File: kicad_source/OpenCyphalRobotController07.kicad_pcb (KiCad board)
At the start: 2 copper layers, 100 x 60 mm, 107 parts, among them CN1 ADAFRUIT_FEATHER, P1 WR-TBL_691313710002, P2 WR-TBL_691322310002, P3 WR-TBL_691313710002, P4 WR-TBL_691313710002, Q1 2N7002, Q2 IPD90P03P4L- 04, U1 IFX007T, U2 74xx08, U3 IFX007T, U4 IFX007T, U5 IFX007T, U6 OPA2374AIDCN, U7 OPA2374AIDCN, U8 ADS1015, U9 IFX91041EFJ

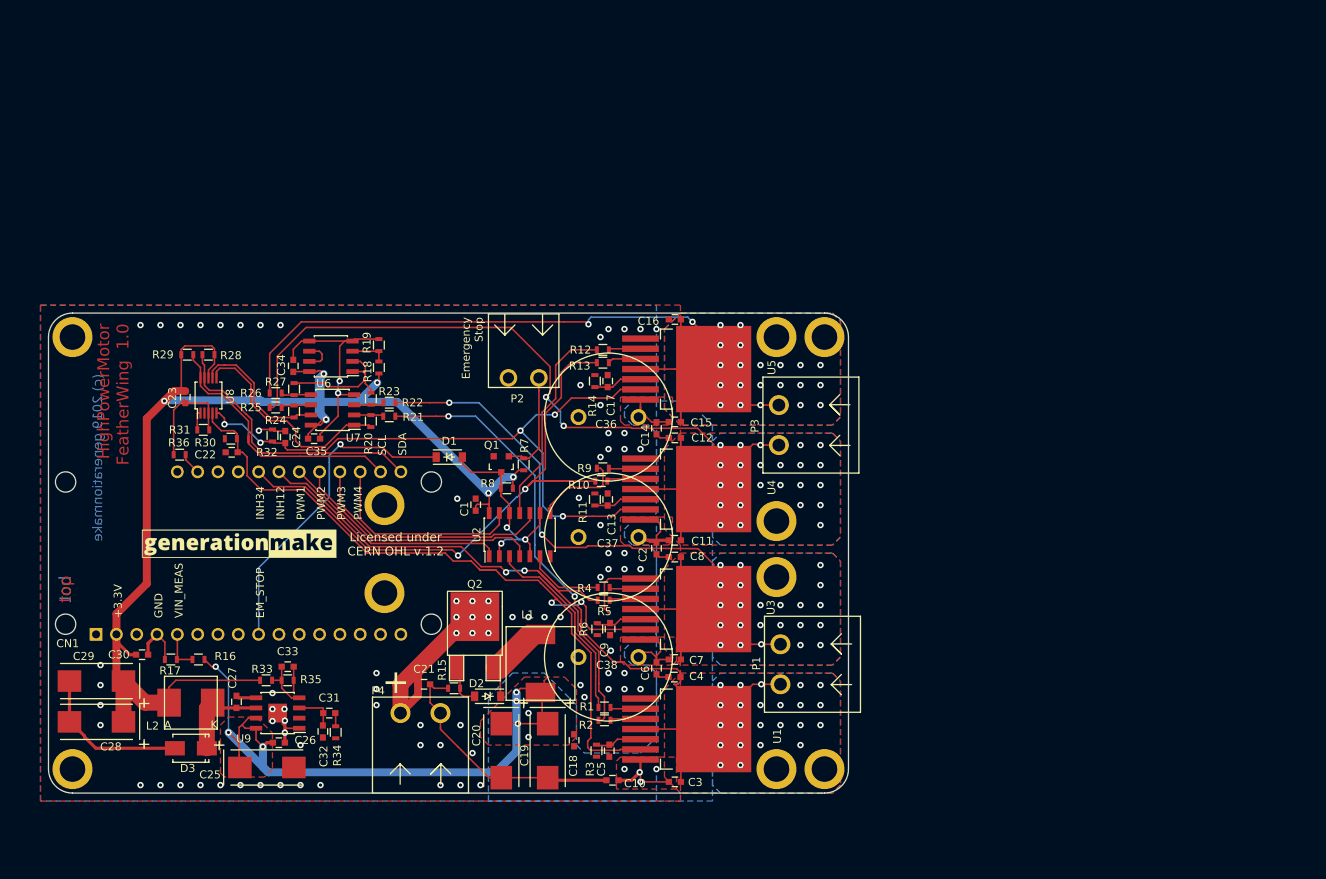
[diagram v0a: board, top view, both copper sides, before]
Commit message: updated layout
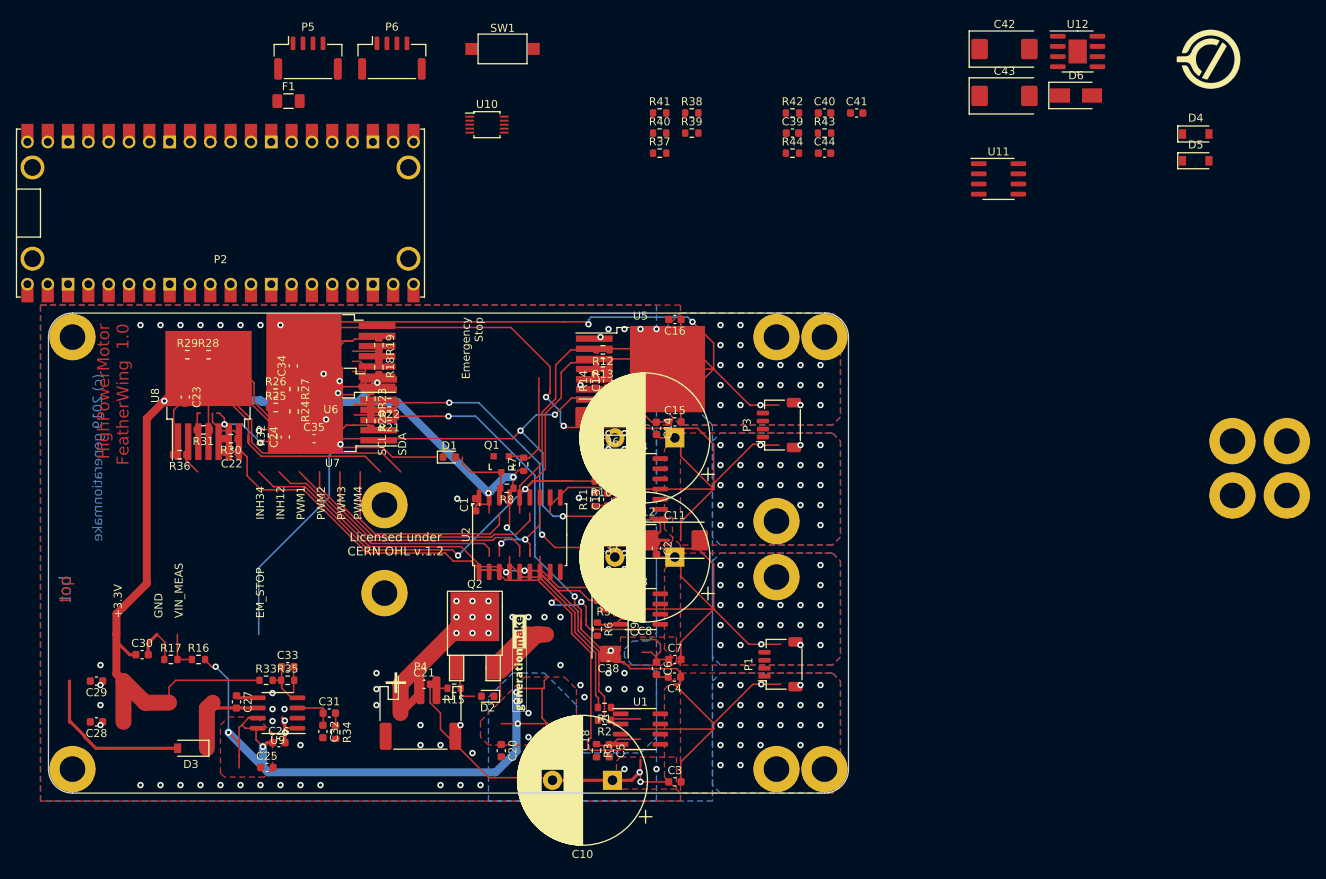
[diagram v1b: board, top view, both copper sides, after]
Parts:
- removed CN1: ADAFRUIT_FEATHER, MODULE_compute:ADAFRUIT_FEATHER_HOLES
- removed G*** (x2): generationmake_logo, labels:generationmake_logo
- added C39: 100nF, Capacitor_SMD:C_0603_1608Metric, F.Cu at (144.0, 43.5)
- added C40: 470pF, Capacitor_SMD:C_0603_1608Metric, F.Cu at (148.0, 41.0)
- added C41: 220nF, Capacitor_SMD:C_0603_1608Metric, F.Cu at (152.0, 41.0)
- added C42: 330uF 6.3V, Capacitor_Tantalum_SMD:CP_EIA-7343-15_Kemet-W, F.Cu at (170.5, 33.0)
- added C43: 330uF 6.3V, Capacitor_Tantalum_SMD:CP_EIA-7343-15_Kemet-W, F.Cu at (170.5, 38.9)
- added C44: 100nF, Capacitor_SMD:C_0603_1608Metric, F.Cu at (148.0, 46.0)
- added D4: 10V, Diode_SMD:D_SOD-123, F.Cu at (194.4, 43.6)
- added D5: BAT46W, Diode_SMD:D_SOD-123, F.Cu at (194.4, 47.0)
- added D6: SSA34, Diode_SMD:D_SMA, F.Cu at (179.4, 38.8)
- added F1: nanoSMDC050F, Fuse:Fuse_1206_3216Metric, F.Cu at (81.0, 39.5)
- added L3: Label, generationmake:opencyphal_small, F.Cu at (196.0, 34.3)
- added MECH11: MHP_3.2_5.0, generationmake:MHP_3.2_5.8, F.Cu at (199.0, 82.0)
- added MECH12: MHP_3.2_5.0, generationmake:MHP_3.2_5.8, F.Cu at (199.0, 88.8)
- added MECH13: MHP_3.2_5.0, generationmake:MHP_3.2_5.8, F.Cu at (205.8, 82.0)
- added MECH14: MHP_3.2_5.0, generationmake:MHP_3.2_5.8, F.Cu at (205.8, 88.8)
- added P5: SM04B-GHS-TB, Connector_JST:JST_GH_SM04B-GHS-TB_1x04-1MP_P1.25mm_Horizontal, F.Cu at (83.4, 34.1)
- added P6: SM04B-GHS-TB, Connector_JST:JST_GH_SM04B-GHS-TB_1x04-1MP_P1.25mm_Horizontal, F.Cu at (93.9, 34.1)
- added R37: 2k2, Resistor_SMD:R_0603_1608Metric, F.Cu at (127.4, 46.0)
- added R38: 2k2, Resistor_SMD:R_0603_1608Metric, F.Cu at (131.4, 41.0)
- added R39: 2k2, Resistor_SMD:R_0603_1608Metric, F.Cu at (131.4, 43.5)
- added R40: 150k, Resistor_SMD:R_0603_1608Metric, F.Cu at (127.4, 43.5)
- added R41: 10k, Resistor_SMD:R_0603_1608Metric, F.Cu at (127.4, 41.0)
- added R42: 22k, Resistor_SMD:R_0603_1608Metric, F.Cu at (144.0, 41.0)
- added R43: 10k, Resistor_SMD:R_0603_1608Metric, F.Cu at (148.0, 43.5)
- added R44: 2k2, Resistor_SMD:R_0603_1608Metric, F.Cu at (144.0, 46.0)
- added SW1: PTS636 SM43 SMTR LFS, Button_Switch_SMD:SW_SPST_CK_RS282G05A3, F.Cu at (107.8, 33.0)
- added U10: ADS1015IDGS, Package_SO:TSSOP-10_3x3mm_P0.5mm, F.Cu at (105.8, 42.5)
- added U11: OPA2374AIDCN, Package_SO:SOIC-8_3.9x4.9mm_P1.27mm, F.Cu at (169.8, 49.2)
- added U12: IFX91041EFJ, Package_SO:SOIC-8-1EP_3.9x4.9mm_P1.27mm_EP2.29x3mm, F.Cu at (179.6, 33.3)
- C1, C13, C14, C17, C18, C2, C30, C35, C6: footprint capacitors:C_0603 -> Capacitor_SMD:C_0603_1608Metric
- C10: value 100nF -> 1000uF 50V; footprint capacitors:C_0603 -> Capacitor_THT:CP_Radial_D16.0mm_P7.50mm
- C11: value 220nF -> 47uF 50V; footprint capacitors:C_0603 -> Capacitor_Tantalum_SMD:CP_EIA-7343-15_Kemet-W
- C12, C8: value 220nF -> 1000uF 50V; footprint capacitors:C_0603 -> Capacitor_THT:CP_Radial_D16.0mm_P7.50mm
- C15, C16, C27, C3, C7: value 220nF -> 100nF; footprint capacitors:C_0603 -> Capacitor_SMD:C_0603_1608Metric
- C19, C20, C25: value 47uF 50V -> 220nF; footprint capacitors:TantalC_SizeD_EIA-7343_Wave -> Capacitor_SMD:C_0603_1608Metric
- C21, C23, C26: value 100nF -> 220nF; footprint capacitors:C_0603 -> Capacitor_SMD:C_0603_1608Metric
- C22, C24: value 1nF -> 220nF; footprint capacitors:C_0603 -> Capacitor_SMD:C_0603_1608Metric
- C28, C29: value 330uF 6.3V -> 100nF; footprint capacitors:TantalC_SizeD_EIA-7343_Wave -> Capacitor_SMD:C_0603_1608Metric
- C31: value 22nF -> 100nF; footprint capacitors:C_0603 -> Capacitor_SMD:C_0603_1608Metric
- C32: value DNI -> 100nF; footprint capacitors:C_0603 -> Capacitor_SMD:C_0603_1608Metric
- C33: value 470pF -> 1nF; footprint capacitors:C_0603 -> Capacitor_SMD:C_0603_1608Metric
- C34: value 100nF -> 1nF; footprint capacitors:C_0603 -> Capacitor_SMD:C_0603_1608Metric
- C36: value 1000uF 50V -> 47uF 50V; footprint capacitors:C_elec_THT_16x25_RM7.5 -> Capacitor_Tantalum_SMD:CP_EIA-7343-15_Kemet-W
- C37: value 1000uF 50V -> DNI; footprint capacitors:C_elec_THT_16x25_RM7.5 -> Capacitor_SMD:C_0603_1608Metric
- C38: value 1000uF 50V -> 22nF; footprint capacitors:C_elec_THT_16x25_RM7.5 -> Capacitor_SMD:C_0603_1608Metric
- C4: value 220nF -> 10pF; footprint capacitors:C_0603 -> Capacitor_SMD:C_0603_1608Metric
- C5: value 100nF -> 10pF; footprint capacitors:C_0603 -> Capacitor_SMD:C_0603_1608Metric
- C9: value 100nF -> 47uF 50V; footprint capacitors:C_0603 -> Capacitor_Tantalum_SMD:CP_EIA-7343-15_Kemet-W
- D1: value BAT46W -> 150060RS75000; footprint diodes:SOD-123 -> LED_SMD:LED_0603_1608Metric
- D2: value 10V -> 150060YS75000; footprint diodes:SOD-123 -> LED_SMD:LED_0603_1608Metric
- D3: value SSA34 -> MBR0530T; footprint diodes:SMA_Standard -> Diode_SMD:D_SOD-123
- L1: value 744373580022 -> Label; footprint L_power:WE-LHMI80xx -> generationmake:generationmake_small_silk
- L2: value 74437346220 -> Label; footprint L_power:WE-LHMI70xx -> generationmake:generationmake_small_solder
- MECH1, MECH2, MECH3, MECH4: value MHP_3.2_5.0 -> MHP_3.2_5.8; footprint MECH_mounting_holes:MHP_3.2_5.0 -> generationmake:MHP_3.2_5.8
- MECH10, MECH5, MECH6, MECH7, MECH8, MECH9: footprint MECH_mounting_holes:MHP_3.2_5.0 -> generationmake:MHP_3.2_5.8
- P1, P3: value WR-TBL_691313710002 -> SM04B-SRSS-TB; footprint CON_wuerth:WR-TBL_691313710002 -> Connector_JST:JST_SH_SM04B-SRSS-TB_1x04-1MP_P1.00mm_Horizontal
- P2: value WR-TBL_691322310002 -> RASPBERRYPI_PICO; footprint CON_wuerth:WR-TBL_691322310002 -> generationmake:RASPI_PICO_SOLDER_ONLY
- P4: value WR-TBL_691313710002 -> S3B-PH-SM4-TB; footprint CON_wuerth:WR-TBL_691313710002 -> Connector_JST:JST_PH_S3B-PH-SM4-TB_1x03-1MP_P2.00mm_Horizontal
- R1, R10, R12, R13, R15, R17, R18, R19, R2, R28, R30, R4, R7, R8, R9: footprint resistors:R_0603 -> Resistor_SMD:R_0603_1608Metric
- R11, R14: value 510 -> 10k; footprint resistors:R_0603 -> Resistor_SMD:R_0603_1608Metric
- R16: value 150k -> 10k; footprint resistors:R_0603 -> Resistor_SMD:R_0603_1608Metric
- R20, R27: value 2k2 -> 10k; footprint resistors:R_0603 -> Resistor_SMD:R_0603_1608Metric
- R21, R22: value 56k -> 510; footprint resistors:R_0603 -> Resistor_SMD:R_0603_1608Metric
- R23, R24: value 2k2 -> 510; footprint resistors:R_0603 -> Resistor_SMD:R_0603_1608Metric
- R25, R26: value 56k -> 10k; footprint resistors:R_0603 -> Resistor_SMD:R_0603_1608Metric
- R29: value 10k -> DNI; footprint resistors:R_0603 -> Resistor_SMD:R_0603_1608Metric
- R3: value 510 -> 100k; footprint resistors:R_0603 -> Resistor_SMD:R_0603_1608Metric
- R31: value DNI -> 1k; footprint resistors:R_0603 -> Resistor_SMD:R_0603_1608Metric
- R32: value 1k -> 56k; footprint resistors:R_0603 -> Resistor_SMD:R_0603_1608Metric
- R33: value 10k -> 56k; footprint resistors:R_0603 -> Resistor_SMD:R_0603_1608Metric
- R34: value 22k -> 56k; footprint resistors:R_0603 -> Resistor_SMD:R_0603_1608Metric
- R35: value 2k2 -> 56k; footprint resistors:R_0603 -> Resistor_SMD:R_0603_1608Metric
- R36: value DNI -> 2k2; footprint resistors:R_0603 -> Resistor_SMD:R_0603_1608Metric
- R5: value 10k -> 3k3; footprint resistors:R_0603 -> Resistor_SMD:R_0603_1608Metric
- R6: value 510 -> 3k3; footprint resistors:R_0603 -> Resistor_SMD:R_0603_1608Metric
- U1: value IFX007T -> 24LC64-I/SN; footprint SOT_TO:TO-263-7Lead -> Package_SO:SOIC-8_3.9x4.9mm_P1.27mm
- U2: value 74xx08 -> MCP2515-I/SO; footprint SOIC:SOIC-14_3.9x8.7mm_Pitch1.27mm -> Package_SO:SOIC-18W_7.5x11.6mm_P1.27mm
- U3: value IFX007T -> SN65HVD232; footprint SOT_TO:TO-263-7Lead -> Package_SO:SOIC-8_3.9x4.9mm_P1.27mm
- U4: value IFX007T -> 74xx08; footprint SOT_TO:TO-263-7Lead -> Package_SO:SOIC-14_3.9x8.7mm_P1.27mm
- U5: footprint SOT_TO:TO-263-7Lead -> Package_TO_SOT_SMD:TO-263-7_TabPin8
- U6, U7: value OPA2374AIDCN -> IFX007T; footprint SOIC:SOIC-8_3.9x4.9mm_Pitch1.27mm -> Package_TO_SOT_SMD:TO-263-7_TabPin8
- U8: value ADS1015 -> IFX007T; footprint SSOP:MSOP-10_3x3mm_Pitch0.5mm -> Package_TO_SOT_SMD:TO-263-7_TabPin8
- U9: value IFX91041EFJ -> OPA2374AIDCN; footprint SOIC:SOIC-8-1EP_3.9x4.9mm_Pitch1.27mm -> Package_SO:SOIC-8_3.9x4.9mm_P1.27mm
- moved P2 43.1 mm to (72.5, 53.5), turned to 90 degrees
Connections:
- C1 pad 1: +3V3 -> +3.3V
- C10 pad 1: VIN -> +BATT
- C11 pad 1: VIN -> +BATT
- C11 pad 2: OUT3 -> GND
- C12 pad 1: OUT3 -> +BATT
- C13 pad 1: /MotorDriver/SR3 -> Net-(C13-Pad1)
- C14 pad 1: VIN -> +3.3V
- C15 pad 1: VIN -> /MotorDriver/SR1
- C15 pad 2: OUT4 -> GND
- C16 pad 1: OUT4 -> /MotorDriver/SR2
- C17 pad 1: /MotorDriver/SR4 -> /MotorDriver/SR3
- C18 pad 1: VIN -> /MotorDriver/SR4
- C19 pad 1: VIN -> +BATT
- C19 pad 2: GND -> OUT1
- C2 pad 1: VIN -> /+BATT_MEAS
- C20 pad 1: VIN -> OUT1
- C21 pad 1: Net-(C21-Pad1) -> +BATT
- C21 pad 2: GND -> OUT2
- C22 pad 1: IS12 -> OUT2
- C23 pad 1: +3V3 -> +BATT
- C23 pad 2: GND -> OUT3
- C24 pad 1: IS34 -> OUT3
- C25 pad 1: VIN -> +BATT
- C25 pad 2: GND -> OUT4
- C26 pad 1: VIN -> OUT4
- C27 pad 1: /VoltageRegulator/BDS -> +BATT
- C27 pad 2: /VoltageRegulator/BUO -> GND
- C28 pad 1: +3V3 -> +BATT
- C29 pad 1: +3V3 -> +BATT
- C3 pad 1: VIN -> +3.3V
- C3 pad 2: OUT1 -> GND
- C30 pad 1: +3V3 -> +BATT
- C31 pad 1: /VoltageRegulator/COMP -> +3.3V
- C31 pad 2: Net-(C31-Pad2) -> GND
- C32 pad 1: /VoltageRegulator/COMP -> +3.3V
- C33 pad 1: /VoltageRegulator/FB -> IS12
- C34 pad 1: +3V3 -> IS34
- C35 pad 1: +3V3 -> +3.3V
- C36 pad 1: VIN -> +BATT
- C37 pad 1: VIN -> /VoltageRegulator/COMP
- C38 pad 1: VIN -> /VoltageRegulator/COMP
- C38 pad 2: GND -> Net-(C38-Pad2)
- C4 pad 1: OUT1 -> /MCP2515/MCP2515_OSC2
- C5 pad 1: /MotorDriver/SR1 -> /MCP2515/MCP2515_OSC1
- C6 pad 1: VIN -> +3.3V
- C7 pad 1: VIN -> +BATT
- C7 pad 2: OUT2 -> GND
- C8 pad 1: OUT2 -> +BATT
- C9 pad 1: /MotorDriver/SR2 -> +BATT
- D1 pad 1: EM_STOP_D -> GND
- D1 pad 2: /MotorDriver/EM_STOP_Q -> /LED2_R
- D2 pad 1: Net-(D2-Pad1) -> GND
- D2 pad 2: Net-(D2-Pad2) -> /LED3_R
- D3 pad 1: /VoltageRegulator/BUO -> /MCP2515/CANVCC
- D3 pad 2: GND -> Net-(D3-Pad2)
- MECH1 pad 1: (no net) -> unconnected-(MECH1-Pad1)
- MECH10 pad 1: (no net) -> unconnected-(MECH10-Pad1)
- MECH2 pad 1: (no net) -> unconnected-(MECH2-Pad1)
- MECH3 pad 1: (no net) -> unconnected-(MECH3-Pad1)
- MECH4 pad 1: (no net) -> unconnected-(MECH4-Pad1)
- MECH5 pad 1: (no net) -> unconnected-(MECH5-Pad1)
- MECH6 pad 1: (no net) -> unconnected-(MECH6-Pad1)
- MECH7 pad 1: (no net) -> unconnected-(MECH7-Pad1)
- MECH8 pad 1: (no net) -> unconnected-(MECH8-Pad1)
- MECH9 pad 1: (no net) -> unconnected-(MECH9-Pad1)
- P1 pad 1: OUT1 -> GND
- P1 pad 2: OUT2 -> +3.3V
- P2 pad 1: /MotorDriver/EM_STOP -> /SER_TX
- P2 pad 2: GND -> /SER_RX
- P3 pad 1: OUT3 -> GND
- P3 pad 2: OUT4 -> +3.3V
- P4 pad 1: Net-(C21-Pad1) -> /NEOPIXEL_R
- P4 pad 2: GND -> +5V
- Q2 pad 1: Net-(D2-Pad2) -> Net-(D4-Pad2)
- Q2 pad 2: Net-(C21-Pad1) -> Net-(C13-Pad1)
- Q2 pad 3: Net-(D2-Pad1) -> Net-(D4-Pad1)
- R1 pad 1: /MotorDriver/PWM1_R -> +3.3V
- R1 pad 2: /MotorDriver/PWM1_U -> I2C_SCL
- R10 pad 1: /MotorDriver/INH3_R -> +3.3V
- R10 pad 2: INH34 -> /MotorDriver/EM_STOP
- R11 pad 1: /MotorDriver/SR3 -> Net-(D4-Pad2)
- R12 pad 1: /MotorDriver/PWM4_R -> +3.3V
- R12 pad 2: /MotorDriver/PWM4_U -> /MotorDriver/EM_STOP_Q
- R13 pad 1: /MotorDriver/INH4_R -> /MotorDriver/PWM1_R
- R13 pad 2: INH34 -> /MotorDriver/PWM1_U
- R14 pad 1: /MotorDriver/SR4 -> /MotorDriver/INH1_R
- R14 pad 2: GND -> INH12
- R15 pad 1: Net-(D2-Pad2) -> /MotorDriver/PWM2_R
- R15 pad 2: GND -> /MotorDriver/PWM2_U
- R16 pad 1: VIN_MEAS -> /MotorDriver/INH2_R
- R16 pad 2: VIN -> INH12
- R17 pad 1: GND -> /MotorDriver/PWM3_R
- R17 pad 2: VIN_MEAS -> /MotorDriver/PWM3_U
- R18 pad 1: /Measurement/VREF_IN -> /MotorDriver/INH3_R
- R18 pad 2: +3V3 -> INH34
- R19 pad 1: GND -> /MotorDriver/PWM4_R
- R19 pad 2: /Measurement/VREF_IN -> /MotorDriver/PWM4_U
- R2 pad 1: /MotorDriver/INH1_R -> +3.3V
- R2 pad 2: INH12 -> I2C_SDA
- R20 pad 1: /Measurement/OUT1R -> /MotorDriver/INH4_R
- R20 pad 2: /Measurement/VS12 -> INH34
- R21 pad 1: OUT1 -> /MotorDriver/SR1
- R21 pad 2: /Measurement/OUT1R -> GND
- R22 pad 1: OUT2 -> /MotorDriver/SR2
- R22 pad 2: /Measurement/OUT2R -> GND
- R23 pad 1: /Measurement/VREF -> /MotorDriver/SR3
- R23 pad 2: /Measurement/OUT2R -> GND
- R24 pad 1: /Measurement/OUT3R -> /MotorDriver/SR4
- R24 pad 2: /Measurement/VS34 -> GND
- R25 pad 1: OUT3 -> /Measurement/VREF_IN
- R25 pad 2: /Measurement/OUT3R -> +3.3V
- R26 pad 1: OUT4 -> GND
- R26 pad 2: /Measurement/OUT4R -> /Measurement/VREF_IN
- R27 pad 1: /Measurement/VREF -> I2C_SDA
- R27 pad 2: /Measurement/OUT4R -> +3.3V
- R28 pad 1: I2C_SDA -> +3.3V
- R28 pad 2: +3V3 -> I2C_SCL
- R29 pad 1: +3V3 -> GND
- R29 pad 2: I2C_SCL -> /Measurement/ADDR
- R3 pad 1: /MotorDriver/SR1 -> +5V
- R3 pad 2: GND -> /+BATT_MEAS
- R31 pad 1: GND -> IS34
- R31 pad 2: /Measurement/ADDR -> GND
- R32 pad 1: IS34 -> OUT1
- R32 pad 2: GND -> /Measurement/OUT1R
- R33 pad 1: +3V3 -> OUT2
- R33 pad 2: /VoltageRegulator/FB -> /Measurement/OUT2R
- R34 pad 1: Net-(C31-Pad2) -> OUT3
- R34 pad 2: GND -> /Measurement/OUT3R
- R35 pad 1: /VoltageRegulator/FB -> OUT4
- R35 pad 2: GND -> /Measurement/OUT4R
- R36 pad 1: /EN -> /Measurement/VREF
- R36 pad 2: GND -> /Measurement/OUT2R
- R4 pad 1: /MotorDriver/PWM2_R -> /+BATT_MEAS
- R4 pad 2: /MotorDriver/PWM2_U -> GND
- R5 pad 1: /MotorDriver/INH2_R -> /LED2
- R5 pad 2: INH12 -> /LED2_R
- R6 pad 1: /MotorDriver/SR2 -> /LED3
- R6 pad 2: GND -> /LED3_R
- R7 pad 1: +3V3 -> +3.3V
- R7 pad 2: /MotorDriver/EM_STOP -> MCP2515_INT
- R8 pad 1: +3V3 -> +3.3V
- R8 pad 2: /MotorDriver/EM_STOP_Q -> MCP2515_CS
- R9 pad 1: /MotorDriver/PWM3_R -> +3.3V
- R9 pad 2: /MotorDriver/PWM3_U -> /MCP2515/MCP2515_RESET
- U1 pad 2: /MotorDriver/PWM1_R -> GND
- U1 pad 3: /MotorDriver/INH1_R -> GND
- U1 pad 4: OUT1 -> GND
- U1 pad 5: /MotorDriver/SR1 -> I2C_SDA
- U1 pad 6: IS12 -> I2C_SCL
- U1 pad 7: VIN -> GND
- U1 pad 8: OUT1 -> +3.3V
- U2 pad 1: PWM1 -> /MCP2515/TXCAN
- U2 pad 10: PWM3 -> /MCP2515/MCP2515_RX1BUF
- U2 pad 11: /MotorDriver/PWM4_U -> /MCP2515/MCP2515_RX0BUF
- U2 pad 12: /MotorDriver/EM_STOP_Q -> MCP2515_INT
- U2 pad 13: PWM4 -> SCK
- U2 pad 14: +3V3 -> MOSI
- U2 pad 2: /MotorDriver/EM_STOP_Q -> /MCP2515/RXCAN
- U2 pad 3: /MotorDriver/PWM1_U -> /MCP2515/MCP2515_SOF
- U2 pad 4: PWM2 -> /MCP2515/MCP2515_TX0RTS
- U2 pad 5: /MotorDriver/EM_STOP_Q -> /MCP2515/MCP2515_TX1RTS
- U2 pad 6: /MotorDriver/PWM2_U -> /MCP2515/MCP2515_TX2RTS
- U2 pad 7: GND -> /MCP2515/MCP2515_OSC2
- U2 pad 8: /MotorDriver/PWM3_U -> /MCP2515/MCP2515_OSC1
- U2 pad 9: /MotorDriver/EM_STOP_Q -> GND
- U3 pad 1: GND -> /MCP2515/TXCAN
- U3 pad 2: /MotorDriver/PWM2_R -> GND
- U3 pad 3: /MotorDriver/INH2_R -> +3.3V
- U3 pad 4: OUT2 -> /MCP2515/RXCAN
- U3 pad 5: /MotorDriver/SR2 -> unconnected-(U3-Pad5)
- U3 pad 6: IS12 -> /MCP2515/CANL
- U3 pad 7: VIN -> /MCP2515/CANH
- U3 pad 8: OUT2 -> GND
- U4 pad 1: GND -> PWM1
- U4 pad 2: /MotorDriver/PWM3_R -> /MotorDriver/EM_STOP_Q
- U4 pad 3: /MotorDriver/INH3_R -> /MotorDriver/PWM1_U
- U4 pad 4: OUT3 -> PWM2
- U4 pad 5: /MotorDriver/SR3 -> /MotorDriver/EM_STOP_Q
- U4 pad 6: IS34 -> /MotorDriver/PWM2_U
- U4 pad 7: VIN -> GND
- U4 pad 8: OUT3 -> /MotorDriver/PWM3_U
- U5 pad 2: /MotorDriver/PWM4_R -> /MotorDriver/PWM1_R
- U5 pad 3: /MotorDriver/INH4_R -> /MotorDriver/INH1_R
- U5 pad 4: OUT4 -> OUT1
- U5 pad 5: /MotorDriver/SR4 -> /MotorDriver/SR1
- U5 pad 6: IS34 -> IS12
- U5 pad 7: VIN -> +BATT
- U5 pad 8: OUT4 -> OUT1
- U6 pad 1: /Measurement/VREF -> GND
- U6 pad 2: /Measurement/VREF -> /MotorDriver/PWM2_R
- U6 pad 3: /Measurement/VREF_IN -> /MotorDriver/INH2_R
- U6 pad 4: GND -> OUT2
- U6 pad 5: GND -> /MotorDriver/SR2
- U6 pad 6: /Measurement/OPA_R -> IS12
- U6 pad 7: /Measurement/OPA_R -> +BATT
- U6 pad 8: +3V3 -> OUT2
- U7 pad 1: /Measurement/VS12 -> GND
- U7 pad 2: /Measurement/OUT1R -> /MotorDriver/PWM3_R
- U7 pad 3: /Measurement/OUT2R -> /MotorDriver/INH3_R
- U7 pad 4: GND -> OUT3
- U7 pad 5: /Measurement/OUT4R -> /MotorDriver/SR3
- U7 pad 6: /Measurement/OUT3R -> IS34
- U7 pad 7: /Measurement/VS34 -> +BATT
- U7 pad 8: +3V3 -> OUT3
- U8 pad 1: /Measurement/ADDR -> GND
- U8 pad 2: (no net) -> /MotorDriver/PWM4_R
- U8 pad 3: GND -> /MotorDriver/INH4_R
- U8 pad 4: IS12 -> OUT4
- U8 pad 5: IS34 -> /MotorDriver/SR4
- U8 pad 6: /Measurement/VS12 -> IS34
- U8 pad 7: /Measurement/VS34 -> +BATT
- U8 pad 8: +3V3 -> OUT4
- U9 pad 1: GND -> /Measurement/VREF
- U9 pad 2: GND -> /Measurement/VREF
- U9 pad 3: /VoltageRegulator/COMP -> /Measurement/VREF_IN
- U9 pad 4: /VoltageRegulator/FB -> GND
- U9 pad 5: /VoltageRegulator/BDS -> GND
- U9 pad 6: /VoltageRegulator/BUO -> /Measurement/OPA_R
- U9 pad 7: VIN -> /Measurement/OPA_R
- U9 pad 8: VIN -> +3.3V
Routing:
- net GND: track 133.3 -> 1386.4 mm, vias 78 -> 113
- net +3V3: track 168.5 -> 0.00 mm, vias 6 -> 0
- net VIN: track 132.2 -> 0.00 mm, vias 12 -> 0
- net OUT3: track 114.8 -> 1.67 mm, vias 26 -> 22
- net IS12: track 100.8 -> 0.00 mm, vias 2 -> 0
- net OUT1: track 96.9 -> 0.00 mm, vias 25 -> 21
- net OUT2: track 94.5 -> 0.00 mm, vias 25 -> 21
- net IS34: track 82.6 -> 0.00 mm, vias 5 -> 0
- net INH34: track 78.2 -> 0.00 mm, vias 2 -> 0
- net INH12: track 69.5 -> 0.00 mm, vias 2 -> 0
- net EM_STOP_D: track 40.7 -> 0.00 mm, vias 1 -> 0
- net I2C_SCL: track 34.8 -> 0.00 mm, vias 0 -> 2
- net I2C_SDA: track 34.7 -> 0.00 mm
- net Net-(C21-Pad1): track 33.7 -> 0.00 mm, vias 9 -> 0
- net Net-(C13-Pad1): track 0.00 -> 33.7 mm, vias 0 -> 9
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- added copper zone on B.Cu, net +BATT
- added copper zone on F.Cu, net +BATT
- added copper zone on F.Cu, net /MotorDriver/SR1
- added copper zone on F.Cu, net /MotorDriver/SR4
- added copper zone on B.Cu, net Net-(C13-Pad1)
- removed copper zone on B.Cu, net Net-(C21-Pad1)
- removed copper zone on B.Cu, net VIN
- removed copper zone on F.Cu, net VIN
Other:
- net class ANTENNA removed
- net class Default removed

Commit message: started layout
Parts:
- removed P1, P3: SM04B-SRSS-TB, Connector_JST:JST_SH_SM04B-SRSS-TB_1x04-1MP_P1.00mm_Horizontal
- removed P2: RASPBERRYPI_PICO, generationmake:RASPI_PICO_SOLDER_ONLY
- removed P4: S3B-PH-SM4-TB, Connector_JST:JST_PH_S3B-PH-SM4-TB_1x03-1MP_P2.00mm_Horizontal
- removed P5, P6: SM04B-GHS-TB, Connector_JST:JST_GH_SM04B-GHS-TB_1x04-1MP_P1.25mm_Horizontal
- removed Q1: 2N7002, SOT_TO:SOT-23
- removed Q2: IPD90P03P4L- 04, SOT_TO:TO-252-2Lead
- added C45: 100nF, Capacitor_SMD:C_0603_1608Metric, F.Cu at (144.8, -16.4)
- added C46: C_Small, Capacitor_SMD:C_0603_1608Metric, F.Cu at (84.0, 101.1)
- added C47: C_Small, Capacitor_SMD:C_0603_1608Metric, F.Cu at (101.1, 101.2)
- added F2: Fuse_Small, Fuse:Fuseholder_Blade_ATO_Littelfuse_Pudenz_2_Pin, F.Cu at (114.7, 106.2)
- added J1: SM04B-SRSS-TB, Connector_JST:JST_SH_SM04B-SRSS-TB_1x04-1MP_P1.00mm_Horizontal, F.Cu at (177.9, 72.7)
- added J11: PowerPole, generationmake:POWERPOLE_2, F.Cu at (119.6, 116.0)
- added J12: Conn_01x02, Connector_Phoenix_MC:PhoenixContact_MCV_1,5_2-G-3.81_1x02_P3.81mm_Vertical, F.Cu at (45.6, 98.6)
- added J13: Conn_01x02, Connector_Phoenix_MC:PhoenixContact_MCV_1,5_2-G-3.81_1x02_P3.81mm_Vertical, F.Cu at (77.8, 116.0)
- added J14: Conn_01x02, Connector_Phoenix_MC:PhoenixContact_MCV_1,5_2-G-3.81_1x02_P3.81mm_Vertical, F.Cu at (95.7, 116.2)
- added J2: RASPBERRYPI_PICO, generationmake:RASPI_PICO_SOLDER_ONLY, F.Cu at (125.4, 69.8)
- added J3: SM04B-SRSS-TB, Connector_JST:JST_SH_SM04B-SRSS-TB_1x04-1MP_P1.00mm_Horizontal, F.Cu at (138.3, 52.8)
- added J4: S3B-PH-SM4-TB, Connector_JST:JST_PH_S3B-PH-SM4-TB_1x03-1MP_P2.00mm_Horizontal, F.Cu at (90.0, 56.0)
- added J5: SM04B-GHS-TB, Connector_JST:JST_GH_SM04B-GHS-TB_1x04-1MP_P1.25mm_Horizontal, F.Cu at (62.1, 76.7)
- added J6: SM04B-GHS-TB, Connector_JST:JST_GH_SM04B-GHS-TB_1x04-1MP_P1.25mm_Horizontal, F.Cu at (60.9, 64.6)
- added R45: 2k2, Resistor_SMD:R_0603_1608Metric, F.Cu at (166.3, -42.3)
- added R46: R_Small, Resistor_SMD:R_0603_1608Metric, F.Cu at (74.8, 107.7)
- added R47: R_Small, Resistor_SMD:R_0603_1608Metric, F.Cu at (92.5, 108.1)
- added U13: IFX91041EFJ, Package_SO:SOIC-8-1EP_3.9x4.9mm_P1.27mm_EP2.29x3mm, F.Cu at (71.8, 94.8)
- added U14: ITS4200S-ME-P, Package_TO_SOT_SMD:SOT-223, F.Cu at (80.6, 106.1)
- added U15: ITS4200S-ME-P, Package_TO_SOT_SMD:SOT-223, F.Cu at (98.2, 106.7)
- C10, C12: value 1000uF 50V -> 100nF; footprint Capacitor_THT:CP_Radial_D16.0mm_P7.50mm -> Capacitor_SMD:C_0603_1608Metric
- C11: value 47uF 50V -> 100nF; footprint Capacitor_Tantalum_SMD:CP_EIA-7343-15_Kemet-W -> Capacitor_SMD:C_0603_1608Metric
- C15, C16, C17, C18: value 100nF -> 220nF
- C23, C24, C25, C26: value 220nF -> 100nF
- C29, C30: value 100nF -> 1nF
- C33: value 1nF -> 47uF 50V; footprint Capacitor_SMD:C_0603_1608Metric -> Capacitor_Tantalum_SMD:CP_EIA-7343-15_Kemet-W
- C34: value 1nF -> 100nF
- C35: value 100nF -> 47uF 50V; footprint Capacitor_SMD:C_0603_1608Metric -> Capacitor_Tantalum_SMD:CP_EIA-7343-15_Kemet-W
- C40: value 470pF -> 100nF
- C41: value 220nF -> 470pF
- C42: value 330uF 6.3V -> 220nF; footprint Capacitor_Tantalum_SMD:CP_EIA-7343-15_Kemet-W -> Capacitor_SMD:C_0603_1608Metric
- C44: value 100nF -> 330uF 6.3V; footprint Capacitor_SMD:C_0603_1608Metric -> Capacitor_Tantalum_SMD:CP_EIA-7343-15_Kemet-W
- C7: value 100nF -> 1000uF 50V; footprint Capacitor_SMD:C_0603_1608Metric -> Capacitor_THT:CP_Radial_D16.0mm_P7.50mm
- C9: value 47uF 50V -> 1000uF 50V; footprint Capacitor_Tantalum_SMD:CP_EIA-7343-15_Kemet-W -> Capacitor_THT:CP_Radial_D16.0mm_P7.50mm
- D4: value 10V -> BAT46W
- D5: value BAT46W -> 10V
- R20: value 10k -> 510
- R24: value 510 -> 10k
- R28: value 10k -> DNI
- R29: value DNI -> 1k
- R31: value 1k -> 56k
- R35: value 56k -> 2k2
- R39: value 2k2 -> 0R
- R40: value 150k -> 0R
- R41: value 10k -> 10m; footprint Resistor_SMD:R_0603_1608Metric -> Resistor_SMD:R_1206_3216Metric
- R42: value 22k -> 10k
- R43: value 10k -> 22k
- R44: value 2k2 -> 10k
- U12: value IFX91041EFJ -> INA226; footprint Package_SO:SOIC-8-1EP_3.9x4.9mm_P1.27mm_EP2.29x3mm -> Package_SO:MSOP-10_3x3mm_P0.5mm
- moved MECH2 293.0 mm to (306.0, -26.6)
- moved C28 289.4 mm to (316.6, -10.8), turned to 0 degrees
- moved C29 286.2 mm to (313.1, -15.8), turned to 0 degrees
- moved L2 283.4 mm to (309.2, -35.5), turned to 0 degrees
- moved MECH1 283.3 mm to (319.6, -29.7)
- moved C30 272.8 mm to (308.6, -9.36)
- moved C31 264.7 mm to (317.1, -13.3)
- moved R33 263.9 mm to (312.6, -9.36)
- moved C27 262.6 mm to (308.6, -4.34), turned to 0 degrees
- moved R35 259.2 mm to (312.6, -4.34)
- moved R31 257.6 mm to (312.6, -6.85), turned to 0 degrees
- moved R30 257.4 mm to (313.1, -13.3), turned to 0 degrees
- moved C25 255.0 mm to (283.9, -28.0)
- moved R24 255.0 mm to (320.6, -10.8), turned to 0 degrees
- moved R36 254.8 mm to (304.6, -9.36), turned to 0 degrees
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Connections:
- C10 pad 1: +BATT -> +3.3V
- C11 pad 1: +BATT -> /MotorDriver/SR1
- C12 pad 1: +BATT -> /MotorDriver/SR2
- C13 pad 1: Net-(C13-Pad1) -> /MotorDriver/SR3
- C14 pad 1: +3.3V -> /MotorDriver/SR4
- C15 pad 1: /MotorDriver/SR1 -> +BATT
- C15 pad 2: GND -> OUT1
- C16 pad 1: /MotorDriver/SR2 -> OUT1
- C17 pad 1: /MotorDriver/SR3 -> +BATT
- C17 pad 2: GND -> OUT2
- C18 pad 1: /MotorDriver/SR4 -> OUT2
- C19 pad 2: OUT1 -> OUT3
- C20 pad 1: OUT1 -> OUT3
- C21 pad 2: OUT2 -> OUT4
- C22 pad 1: OUT2 -> OUT4
- C23 pad 2: OUT3 -> GND
- C24 pad 1: OUT3 -> +BATT
- C25 pad 2: OUT4 -> GND
- C26 pad 1: OUT4 -> +BATT
- C27 pad 1: +BATT -> +3.3V
- C28 pad 1: +BATT -> +3.3V
- C29 pad 1: +BATT -> IS12
- C30 pad 1: +BATT -> IS34
- C32 pad 1: +3.3V -> +BATT
- C33 pad 1: IS12 -> +BATT
- C34 pad 1: IS34 -> +3V3
- C35 pad 1: +3.3V -> +BATT
- C40 pad 1: /VoltageRegulator/FB -> Net-(C40-Pad1)
- C41 pad 1: /VoltageRegulator/BDS -> /VoltageRegulator/FB
- C41 pad 2: /VoltageRegulator/BUO -> GND
- C42 pad 1: +5V -> /VoltageRegulator/BDS
- C42 pad 2: GND -> /VoltageRegulator/BUO
- D4 pad 1: Net-(D4-Pad1) -> EM_STOP_D
- D4 pad 2: Net-(D4-Pad2) -> /MotorDriver/EM_STOP_Q
- D5 pad 1: EM_STOP_D -> Net-(D5-Pad1)
- D5 pad 2: /MotorDriver/EM_STOP_Q -> Net-(D5-Pad2)
- R11 pad 1: Net-(D4-Pad2) -> +3.3V
- R11 pad 2: GND -> /MotorDriver/EM_STOP_Q
- R12 pad 1: +3.3V -> /MotorDriver/PWM1_R
- R12 pad 2: /MotorDriver/EM_STOP_Q -> /MotorDriver/PWM1_U
- R13 pad 1: /MotorDriver/PWM1_R -> /MotorDriver/INH1_R
- R13 pad 2: /MotorDriver/PWM1_U -> INH12
- R14 pad 1: /MotorDriver/INH1_R -> /MotorDriver/PWM2_R
- R14 pad 2: INH12 -> /MotorDriver/PWM2_U
- R15 pad 1: /MotorDriver/PWM2_R -> /MotorDriver/INH2_R
- R15 pad 2: /MotorDriver/PWM2_U -> INH12
- R16 pad 1: /MotorDriver/INH2_R -> /MotorDriver/PWM3_R
- R16 pad 2: INH12 -> /MotorDriver/PWM3_U
- R17 pad 1: /MotorDriver/PWM3_R -> /MotorDriver/INH3_R
- R17 pad 2: /MotorDriver/PWM3_U -> INH34
- R18 pad 1: /MotorDriver/INH3_R -> /MotorDriver/PWM4_R
- R18 pad 2: INH34 -> /MotorDriver/PWM4_U
- R19 pad 1: /MotorDriver/PWM4_R -> /MotorDriver/INH4_R
- R19 pad 2: /MotorDriver/PWM4_U -> INH34
- R20 pad 1: /MotorDriver/INH4_R -> /MotorDriver/SR1
- R20 pad 2: INH34 -> GND
- R21 pad 1: /MotorDriver/SR1 -> /MotorDriver/SR2
- R22 pad 1: /MotorDriver/SR2 -> /MotorDriver/SR3
- R23 pad 1: /MotorDriver/SR3 -> /MotorDriver/SR4
- R24 pad 1: /MotorDriver/SR4 -> /Measurement/VREF_IN
- R24 pad 2: GND -> +3.3V
- R25 pad 1: /Measurement/VREF_IN -> GND
- R25 pad 2: +3.3V -> /Measurement/VREF_IN
- R26 pad 1: GND -> I2C_SDA
- R26 pad 2: /Measurement/VREF_IN -> +3.3V
- R27 pad 1: I2C_SDA -> +3.3V
- R27 pad 2: +3.3V -> I2C_SCL
- R28 pad 1: +3.3V -> GND
- R28 pad 2: I2C_SCL -> /Measurement/ADDR
- R29 pad 1: GND -> IS12
- R29 pad 2: /Measurement/ADDR -> GND
- R30 pad 1: IS12 -> IS34
- R31 pad 1: IS34 -> OUT1
- R31 pad 2: GND -> /Measurement/OUT1R
- R32 pad 1: OUT1 -> OUT2
- R32 pad 2: /Measurement/OUT1R -> /Measurement/OUT2R
- R33 pad 1: OUT2 -> OUT3
- R33 pad 2: /Measurement/OUT2R -> /Measurement/OUT3R
- R34 pad 1: OUT3 -> OUT4
- R34 pad 2: /Measurement/OUT3R -> /Measurement/OUT4R
- R35 pad 1: OUT4 -> /Measurement/VREF
- R35 pad 2: /Measurement/OUT4R -> /Measurement/OUT2R
- R36 pad 2: /Measurement/OUT2R -> /Measurement/OUT4R
- R37 pad 1: /Measurement/VREF -> /Measurement/OUT1R
- R37 pad 2: /Measurement/OUT4R -> /Measurement/VS12
- R38 pad 1: /Measurement/OUT1R -> /Measurement/OUT3R
- R38 pad 2: /Measurement/VS12 -> /Measurement/VS34
- R39 pad 1: /Measurement/OUT3R -> Net-(R39-Pad1)
- R39 pad 2: /Measurement/VS34 -> GND
- R40 pad 1: VIN_MEAS -> Net-(R40-Pad1)
- R40 pad 2: +BATT -> GND
- R41 pad 1: GND -> +BATT
- R41 pad 2: VIN_MEAS -> Net-(L4-Pad1)
- R42 pad 1: Net-(C38-Pad2) -> Net-(D5-Pad2)
- R43 pad 1: +5V -> Net-(C38-Pad2)
- R43 pad 2: /VoltageRegulator/FB -> GND
- R44 pad 1: /VoltageRegulator/FB -> +5V
- R44 pad 2: GND -> /VoltageRegulator/FB
- U12 pad 1: GND -> Net-(R40-Pad1)
- U12 pad 2: GND -> Net-(R39-Pad1)
- U12 pad 3: /VoltageRegulator/COMP -> unconnected-(U12-Pad3)
- U12 pad 4: /VoltageRegulator/FB -> I2C_SDA
- U12 pad 5: /VoltageRegulator/BDS -> I2C_SCL
- U12 pad 6: /VoltageRegulator/BUO -> +3V3
- U12 pad 7: +BATT -> GND
- U12 pad 8: +BATT -> Net-(L4-Pad1)
- U12 pad 9: GND -> +BATT
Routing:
- net GND: track 1386.4 -> 0.00 mm, vias 113 -> 0
- net OUT4: track 91.9 -> 0.00 mm, vias 15 -> 0
- net Net-(C13-Pad1): track 33.7 -> 0.00 mm, vias 9 -> 0
- net PWM2: track 31.6 -> 0.00 mm
- net MCP2515_CS: track 28.8 -> 0.00 mm, vias 3 -> 0
- net +BATT: track 24.7 -> 0.00 mm, vias 2 -> 0
- net Net-(D3-Pad2): track 19.7 -> 0.00 mm
- net Net-(D4-Pad1): track 18.4 -> 0.00 mm
- net /MCP2515/CANVCC: track 17.4 -> 0.00 mm
- net /MotorDriver/EM_STOP: track 13.2 -> 0.00 mm
- net +3.3V: track 12.8 -> 0.00 mm
- net /MCP2515/MCP2515_RX0BUF: track 11.3 -> 0.00 mm
- net /MotorDriver/EM_STOP_Q: track 10.00 -> 0.00 mm
- net /Measurement/OUT2R: track 6.57 -> 0.00 mm
- net /MotorDriver/PWM3_R: track 6.55 -> 0.00 mm
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- removed copper zone on B.Cu, net +BATT
- removed copper zone on F.Cu, net +BATT
- removed copper zone on F.Cu, net /MotorDriver/SR1
- removed copper zone on F.Cu, net /MotorDriver/SR4
- removed copper zone on B.Cu, net GND
- removed copper zone on F.Cu, net GND
- removed copper zone on B.Cu, net Net-(C13-Pad1)
- removed copper zone on B.Cu, net OUT1
- removed copper zone on F.Cu, net OUT1
- removed copper zone on B.Cu, net OUT2
- removed copper zone on F.Cu, net OUT2
- removed copper zone on B.Cu, net OUT3
- removed copper zone on F.Cu, net OUT3
- removed copper zone on B.Cu, net OUT4
- removed copper zone on F.Cu, net OUT4
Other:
- board outline removed
- board text removed: "+"
- board text removed: "+3.3V"
- board text removed: "10x"
- board text removed: "6x for heatspreader"
- board text removed: "EM_STOP"
- board text removed: "Emergency Stop"
- board text removed: "GND"
- board text removed: "INH12"
- board text removed: "INH34"
- board text removed: "PWM1"
- board text removed: "PWM2"
- board text removed: "PWM3"
- board text removed: "PWM4"
- board text removed: "SCL"
- board text removed: "SDA"
- board text removed: "VIN_MEAS"
- board text removed: "bot"
- board text removed: "top"

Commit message: made first draft of placement
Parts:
- removed R26, R27: 10k, Resistor_SMD:R_0603_1608Metric
- added C48: 100nF, Capacitor_SMD:C_0603_1608Metric, F.Cu at (160.5, 22.5)
- added C49: 100nF, Capacitor_SMD:C_0603_1608Metric, F.Cu at (152.5, 30.0)
- added C50: 100nF, Capacitor_SMD:C_0603_1608Metric, F.Cu at (152.5, 22.5)
- added C51: 22pF, Capacitor_SMD:C_0603_1608Metric, F.Cu at (156.5, 30.0)
- added C52: 22pF, Capacitor_SMD:C_0603_1608Metric, F.Cu at (160.5, 25.0)
- added J10: x, Connector_Phoenix_MC:PhoenixContact_MCV_1,5_2-G-3.81_1x02_P3.81mm_Vertical, F.Cu at (117.5, 123.9)
- added J7: x, Connector_Phoenix_MC:PhoenixContact_MCV_1,5_2-G-3.81_1x02_P3.81mm_Vertical, F.Cu at (196.5, 101.2)
- added J8: x, Connector_Phoenix_MC:PhoenixContact_MCV_1,5_2-G-3.81_1x02_P3.81mm_Vertical, F.Cu at (145.8, 122.7)
- added J9: x, Connector_Phoenix_MC:PhoenixContact_MCV_1,5_2-G-3.81_1x02_P3.81mm_Vertical, F.Cu at (170.7, 123.2)
- added Q1: 2N7002, Package_TO_SOT_SMD:SOT-23, F.Cu at (198.7, 90.6)
- added Q2: IPD90P03P4L- 04, Package_TO_SOT_SMD:TO-252-2, F.Cu at (122.1, 99.7)
- added R48: 0R, Resistor_SMD:R_0603_1608Metric, F.Cu at (156.5, 25.0)
- added R49: 10k, Resistor_SMD:R_0603_1608Metric, F.Cu at (156.5, 27.5)
- added R50: 0R, Resistor_SMD:R_0603_1608Metric, F.Cu at (152.5, 27.5)
- added R51: 0R, Resistor_SMD:R_0603_1608Metric, F.Cu at (148.5, 22.5)
- added R52: 0R, Resistor_SMD:R_0603_1608Metric, F.Cu at (148.5, 25.0)
- added R53: DNI, Resistor_SMD:R_0603_1608Metric, F.Cu at (152.5, 25.0)
- added R54: DNI, Resistor_SMD:R_0603_1608Metric, F.Cu at (148.5, 27.5)
- added R55: DNI, Resistor_SMD:R_0603_1608Metric, F.Cu at (148.5, 30.0)
- added R56: DNI, Resistor_SMD:R_0603_1608Metric, F.Cu at (156.5, 22.5)
- added U16: BNO085, Package_LGA:LGA-28_5.2x3.8mm_P0.5mm, F.Cu at (166.0, 32.0)
- added Y1: RH100-16.000-16-3030-EXT-TR, Crystal:Crystal_SMD_3225-4Pin_3.2x2.5mm, F.Cu at (70.0, 77.5)
- moved R5 237.4 mm to (114.4, 54.3)
- moved C2 234.6 mm to (110.4, 38.2)
- moved R4 228.0 mm to (112.7, 40.5)
- moved C16 222.9 mm to (138.6, 123.1)
- moved C37 222.8 mm to (49.4, 111.6)
- moved R6 221.9 mm to (119.8, 55.6)
- moved C4 221.2 mm to (75.5, 77.5)
- moved C5 218.6 mm to (75.1, 80.0)
- moved R3 216.8 mm to (111.9, 44.1)
- moved C6 215.4 mm to (67.7, 86.3)
- moved D3 214.4 mm to (70.0, 64.1)
- moved C38 207.5 mm to (52.1, 109.2)
- moved C18 206.6 mm to (157.4, 124.0)
- moved C19 204.7 mm to (163.6, 124.0)
- moved D1 204.2 mm to (114.0, 51.4)
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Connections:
- net Net-(C40-Pad1) renamed /VoltageRegulator/+BATT_Q
- net Net-(F2-Pad2) renamed /VoltageRegulator/+BATT_F
- net Net-(L4-Pad1) renamed /VoltageRegulator/+BATT_R
- D5 pad 1: Net-(D5-Pad1) -> /VoltageRegulator/+BATT_I
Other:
- board outline added: 140 x 70 mm

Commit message: made first draft of layout
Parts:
- J5, J6: value SM04B-GHS-TB -> BM04B-GHS-TBT; footprint Connector_JST:JST_GH_SM04B-GHS-TB_1x04-1MP_P1.25mm_Horizontal -> Connector_JST:JST_GH_BM04B-GHS-TBT_1x04-1MP_P1.25mm_Vertical
- moved MECH1 177.4 mm to (55.0, 122.0)
- moved MECH3 164.3 mm to (55.0, 60.0)
- moved MECH7 110.5 mm to (127.0, 112.0)
- moved MECH8 103.1 mm to (121.0, 99.0)
- moved R56 78.1 mm to (124.7, 93.8), turned to -90 degrees
- moved R48 78.0 mm to (114.9, 91.0)
- moved R53 77.6 mm to (114.9, 92.9)
- moved C50 76.3 mm to (115.0, 89.0), turned to 180 degrees
- moved C48 73.1 mm to (126.0, 87.0)
- moved U16 72.6 mm to (121.0, 89.0), turned to -90 degrees
- moved R51 72.6 mm to (115.0, 86.9), turned to 180 degrees
- moved R54 72.1 mm to (118.0, 92.9)
- moved C52 70.4 mm to (131.2, 89.0)
- moved MECH6 70.2 mm to (157.0, 112.0)
- moved R52 68.9 mm to (115.0, 85.3), turned to 180 degrees
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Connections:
- J2 pad 10: PWM2 -> PWM3
- J2 pad 11: PWM3 -> PWM2
- J2 pad 12: PWM4 -> PWM1
- J2 pad 14: INH12 -> INH34
- J2 pad 15: INH34 -> INH12
- J2 pad 9: PWM1 -> PWM4
- J8 pad 1: OUT1 -> OUT2
- J8 pad 2: OUT2 -> OUT1
- J9 pad 1: OUT3 -> OUT4
- J9 pad 2: OUT4 -> OUT3
- U10 pad 3: unconnected-(U10-Pad3) -> GND
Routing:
- net GND: track 0.00 -> 504.7 mm
- net I2C_SCL: track 0.00 -> 107.5 mm
- net I2C_SDA: track 0.00 -> 106.9 mm
- net INH34: track 0.00 -> 101.8 mm, vias 0 -> 2
- net INH12: track 0.00 -> 88.2 mm
- net +BATT: track 0.00 -> 84.1 mm
- net IS12: track 0.00 -> 79.3 mm, vias 0 -> 3
- net OUT1: track 0.00 -> 74.6 mm, vias 0 -> 2
- net PWM3: track 0.00 -> 61.2 mm
- net /MotorDriver/EM_STOP_Q: track 0.00 -> 61.1 mm, vias 0 -> 5
- net PWM2: track 0.00 -> 60.9 mm
- net OUT2: track 0.00 -> 58.9 mm, vias 0 -> 2
- net OUT3: track 0.00 -> 58.1 mm, vias 0 -> 2
- net EM_STOP_D: track 0.00 -> 58.0 mm
- net +3.3V: track 0.00 -> 57.7 mm, vias 0 -> 2
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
